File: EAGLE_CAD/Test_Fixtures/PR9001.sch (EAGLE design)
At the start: 14 parts, among them T10 PR9001_TESTPOINT, T11 PR9001_TESTPOINT, T12 PR9001_TESTPOINT, T13 PR9001_TESTPOINT, T2 PR9001_TESTPOINT, T3 PR9001_TESTPOINT, T4 PR9001_TESTPOINT, T5 PR9001_TESTPOINT

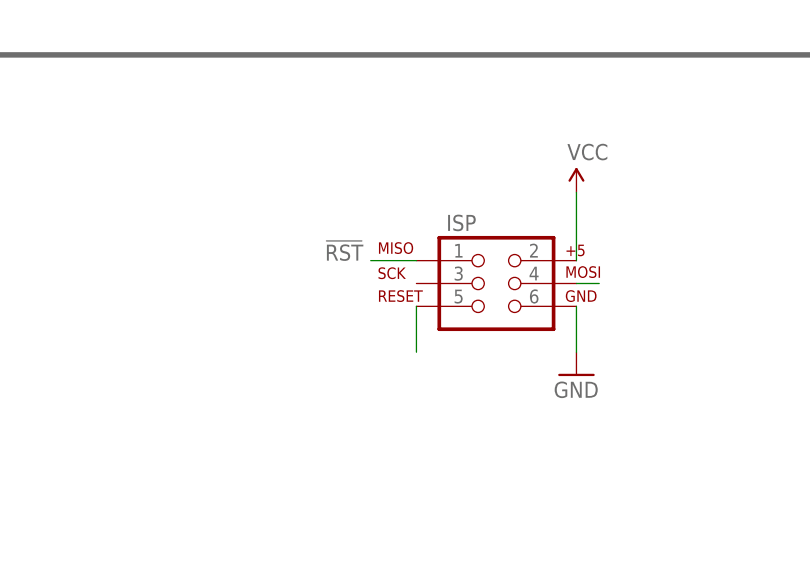
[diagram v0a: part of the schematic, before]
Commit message: PR9001 Programming Fixture
Updated layout and added an additional mounting hole.
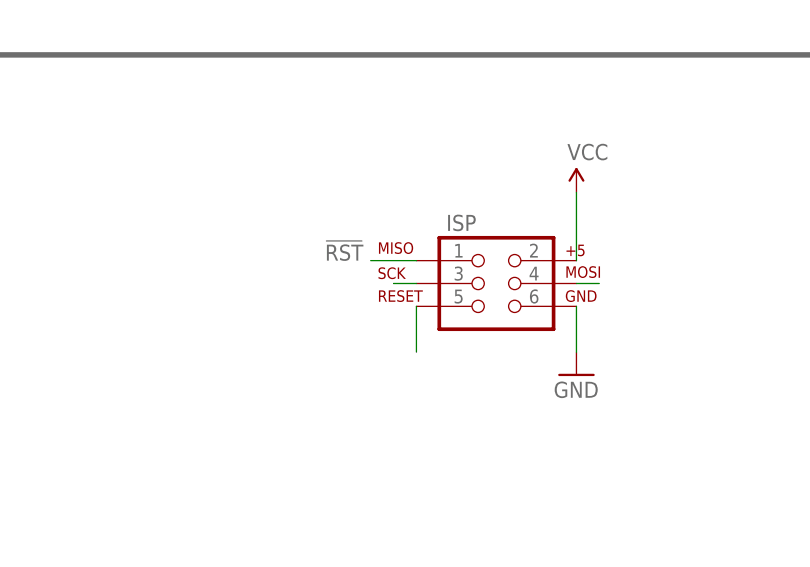
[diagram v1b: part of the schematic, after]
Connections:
- net SCLK: now also ISP.3
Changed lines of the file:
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@@
 <wire x1="76.2" y1="106.68" x2="76.2" y2="104.14" width="0.1524" layer="91"/>
+</segment>
+<segment>
+<pinref part="ISP" gate="G$1" pin="3"/>
+<wire x1="213.36" y1="127" x2="210.82" y2="127" width="0.1524" layer="91"/>
 </segment>
 </net>
